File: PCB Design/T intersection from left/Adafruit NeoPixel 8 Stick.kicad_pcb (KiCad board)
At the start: 2 copper layers, 36.2 x 28.6 mm, 8 parts, among them CN1 1X4SMT, CN2 1X4SMT, CN3 1X4SMT

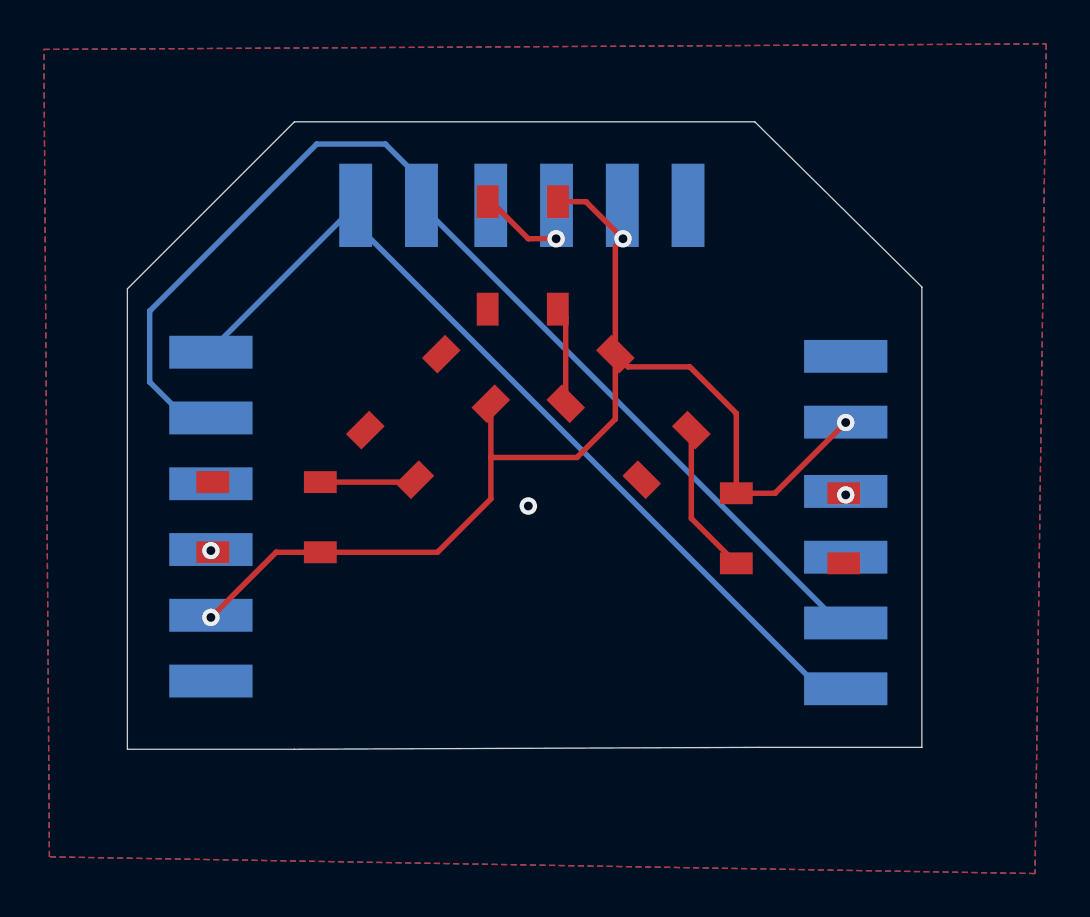
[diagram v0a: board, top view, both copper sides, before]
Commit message: move vias off pads
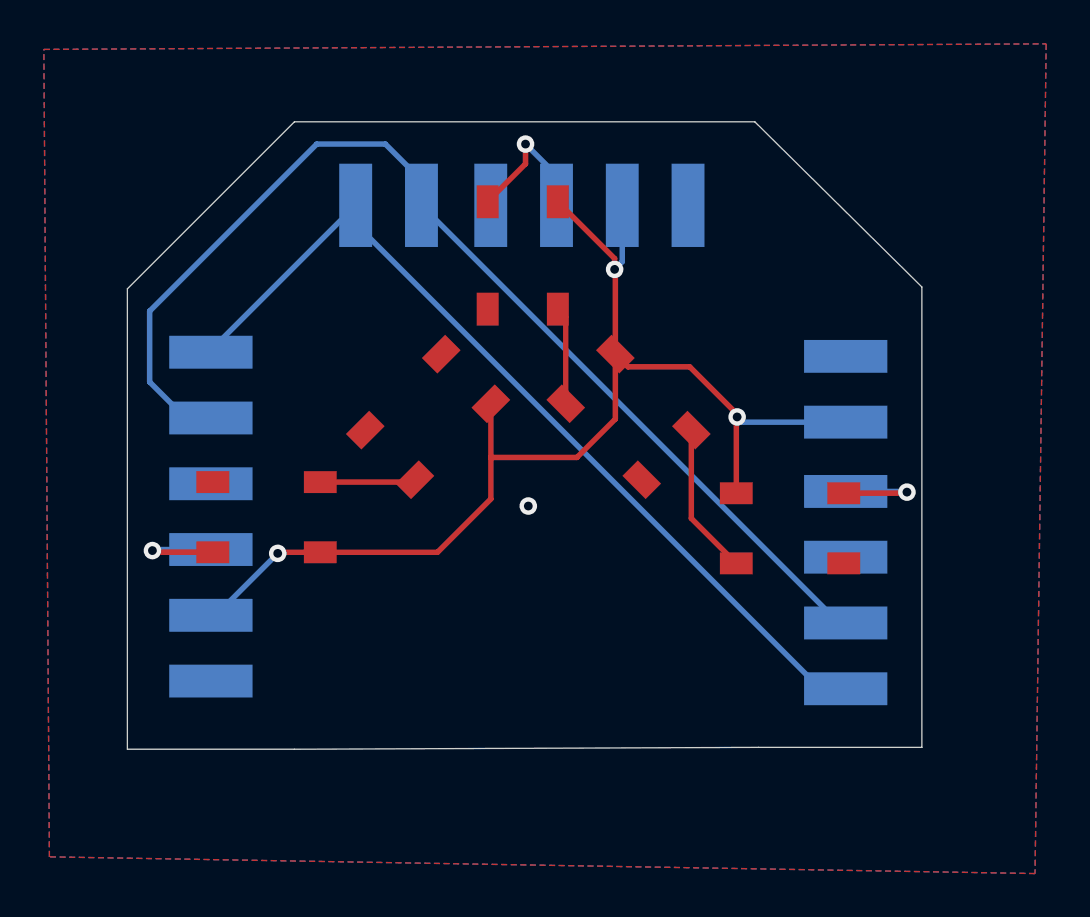
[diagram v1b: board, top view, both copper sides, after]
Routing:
- net Net-(CN2-Pad3): track 0.00 -> 5.71 mm
- net Net-(CN3-Pad3): track 0.00 -> 5.48 mm
- net Net-(CN1-Pad4): track 3.82 -> 6.72 mm
- net +5V: track 54.4 -> 55.2 mm
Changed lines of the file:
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@@
   (gr_line (start 122.428 97.536) (end 130.048 89.915998) (layer "Edge.Cuts") (width 0.05))
   (segment (start 131.228 109.55) (end 136.576 109.55) (width 0.25) (layer "F.Cu") (net 1))
+  (segment (start 144.653 96.153) (end 142.062 93.562) (width 0.25) (layer "F.Cu") (net 1))
   (segment (start 150.204 103.214) (end 148.082 101.092) (width 0.25) (layer "F.Cu") (net 1))
-  (segment (start 144.686959 95.597041) (end 144.686959 100.514218) (width 0.25) (layer "F.Cu") (net 1))
+  (segment (start 144.686959 96.680959) (end 144.653 96.647) (width 0.25) (layer "F.Cu") (net 1))
   (segment (start 136.576 109.55) (end 139.007782 107.118218) (width 0.25) (layer "F.Cu") (net 1))
-  (segment (start 151.968 106.858) (end 150.204 106.858) (width 0.25) (layer "F.Cu") (net 1))
   (segment (start 145.264741 101.092) (end 144.686959 100.514218) (width 0.25) (layer "F.Cu") (net 1))
   (segment (start 144.686959 100.514218) (end 144.686959 103.471041) (width 0.25) (layer "F.Cu") (net 1))
-  (segment (start 126.238 112.522) (end 129.21 109.55) (width 0.25) (layer "F.Cu") (net 1))
+  (segment (start 144.653 96.647) (end 144.653 96.153) (width 0.25) (layer "F.Cu") (net 1))
   (segment (start 139.007782 105.225782) (end 139.007782 102.776959) (width 0.25) (layer "F.Cu") (net 1))
-  (segment (start 142.062 93.562) (end 143.346 93.562) (width 0.25) (layer "F.Cu") (net 1))
   (segment (start 144.686959 103.471041) (end 142.932218 105.225782) (width 0.25) (layer "F.Cu") (net 1))
   (segment (start 148.082 101.092) (end 145.264741 101.092) (width 0.25) (layer "F.Cu") (net 1))
   (segment (start 150.204 106.858) (end 150.204 103.214) (width 0.25) (layer "F.Cu") (net 1))
   (segment (start 129.21 109.55) (end 131.228 109.55) (width 0.25) (layer "F.Cu") (net 1))
+  (segment (start 144.686959 100.514218) (end 144.686959 96.680959) (width 0.25) (layer "F.Cu") (net 1))
   (segment (start 142.932218 105.225782) (end 139.007782 105.225782) (width 0.25) (layer "F.Cu") (net 1))
-  (segment (start 145.034 95.25) (end 144.686959 95.597041) (width 0.25) (layer "F.Cu") (net 1))
-  (segment (start 155.194 103.632) (end 151.968 106.858) (width 0.25) (layer "F.Cu") (net 1))
   (segment (start 139.007782 107.118218) (end 139.007782 105.225782) (width 0.25) (layer "F.Cu") (net 1))
-  (segment (start 143.346 93.562) (end 145.034 95.25) (width 0.25) (layer "F.Cu") (net 1))
-  (via (at 145.034 95.25) (size 0.8) (drill 0.4) (layers "F.Cu" "B.Cu") (net 1))
-  (via (at 126.238 112.522) (size 0.8) (drill 0.4) (layers "F.Cu" "B.Cu") (net 1))
-  (via (at 155.194 103.632) (size 0.8) (drill 0.4) (layers "F.Cu" "B.Cu") (net 1))
+  (via (at 144.653 96.647) (size 0.8) (drill 0.4) (layers "F.Cu" "B.Cu") (net 1))
+  (via (at 129.286 109.601) (size 0.8) (drill 0.4) (layers "F.Cu" "B.Cu") (net 1))
+  (via (at 150.241 103.378) (size 0.8) (drill 0.4) (layers "F.Cu" "B.Cu") (net 1))
+  (segment (start 145.002 96.298) (end 145.002 93.726) (width 0.25) (layer "B.Cu") (net 1))
+  (segment (start 144.653 96.647) (end 145.002 96.298) (width 0.25) (layer "B.Cu") (net 1))
+  (segment (start 155.194 103.616) (end 150.479 103.616) (width 0.25) (layer "B.Cu") (net 1))
+  (segment (start 126.238 112.426) (end 126.461 112.426) (width 0.25) (layer "B.Cu") (net 1))
+  (segment (start 150.479 103.616) (end 150.241 103.378) (width 0.25) (layer "B.Cu") (net 1))
+  (segment (start 126.461 112.426) (end 129.286 109.601) (width 0.25) (layer "B.Cu") (net 1))
   (via (at 140.716 107.442) (size 0.8) (drill 0.4) (layers "F.Cu" "B.Cu") (free) (net 2))
   (segment (start 131.064 90.932) (end 134.198 90.932) (width 0.25) (layer "B.Cu") (net 3))
@@
   (segment (start 135.842 93.726) (end 154.892 112.776) (width 0.25) (layer "B.Cu") (net 3))
   (segment (start 135.842 92.576) (end 135.842 93.726) (width 0.25) (layer "B.Cu") (net 3))
-  (via (at 155.194 106.934) (size 0.8) (drill 0.4) (layers "F.Cu" "B.Cu") (net 4))
+  (segment (start 155.104 106.858) (end 157.937 106.858) (width 0.25) (layer "F.Cu") (net 4))
+  (segment (start 157.937 106.858) (end 157.988 106.807) (width 0.25) (layer "F.Cu") (net 4))
+  (via (at 157.988 106.807) (size 0.8) (drill 0.4) (layers "F.Cu" "B.Cu") (net 4))
+  (segment (start 157.957 106.776) (end 157.988 106.807) (width 0.25) (layer "B.Cu") (net 4))
+  (segment (start 155.194 106.776) (end 157.957 106.776) (width 0.25) (layer "B.Cu") (net 4))
   (segment (start 126.238 100.33) (end 132.842 93.726) (width 0.25) (layer "B.Cu") (net 5))
   (segment (start 132.842 94.574) (end 132.842 93.726) (width 0.25) (layer "B.Cu") (net 5))
@@
   (segment (start 154.044 115.776) (end 132.842 94.574) (width 0.25) (layer "B.Cu") (net 5))
   (segment (start 126.238 100.426) (end 126.238 100.33) (width 0.25) (layer "B.Cu") (net 5))
-  (segment (start 138.862 93.562) (end 139.028 93.562) (width 0.25) (layer "F.Cu") (net 6))
-  (segment (start 139.028 93.562) (end 140.716 95.25) (width 0.25) (layer "F.Cu") (net 6))
-  (segment (start 140.716 95.25) (end 141.986 95.25) (width 0.25) (layer "F.Cu") (net 6))
-  (via (at 141.986 95.25) (size 0.8) (drill 0.4) (layers "F.Cu" "B.Cu") (net 6))
-  (via (at 126.238 109.474) (size 0.8) (drill 0.4) (layers "F.Cu" "B.Cu") (net 7))
+  (segment (start 140.589 91.835) (end 140.589 90.932) (width 0.25) (layer "F.Cu") (net 6))
+  (segment (start 138.862 93.562) (end 140.589 91.835) (width 0.25) (layer "F.Cu") (net 6))
+  (via (at 140.589 90.932) (size 0.8) (drill 0.4) (layers "F.Cu" "B.Cu") (net 6))
+  (segment (start 142.002 93.726) (end 142.002 92.345) (width 0.25) (layer "B.Cu") (net 6))
+  (segment (start 142.002 92.345) (end 140.589 90.932) (width 0.25) (layer "B.Cu") (net 6))
+  (segment (start 123.647 109.55) (end 126.328 109.55) (width 0.25) (layer "F.Cu") (net 7))
+  (segment (start 123.571 109.474) (end 123.647 109.55) (width 0.25) (layer "F.Cu") (net 7))
+  (via (at 123.571 109.474) (size 0.8) (drill 0.4) (layers "F.Cu" "B.Cu") (net 7))
+  (segment (start 123.619 109.426) (end 123.571 109.474) (width 0.25) (layer "B.Cu") (net 7))
+  (segment (start 126.238 109.426) (end 123.619 109.426) (width 0.25) (layer "B.Cu") (net 7))
   (segment (start 150.204 110.058) (end 148.151782 108.005782) (width 0.25) (layer "F.Cu") (net 8))
   (segment (start 148.151782 108.005782) (end 148.151782 103.979041) (width 0.25) (layer "F.Cu") (net 8))
